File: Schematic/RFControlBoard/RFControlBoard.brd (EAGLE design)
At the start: 100 x 49 mm, 22 parts, among them IC1 LM320LZ-XX, U1 ATMEGA328P-PU

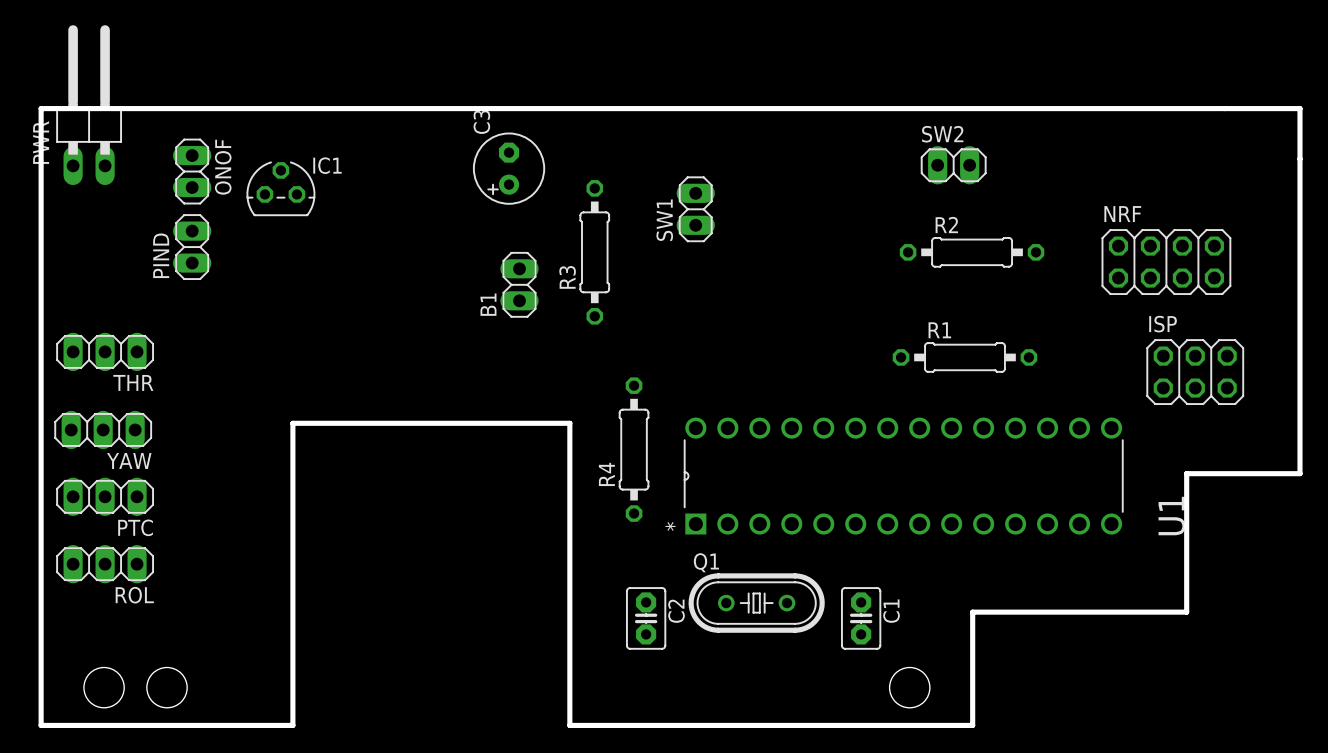
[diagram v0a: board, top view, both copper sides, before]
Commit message: Разведено для однослойной платы + пары проводков.
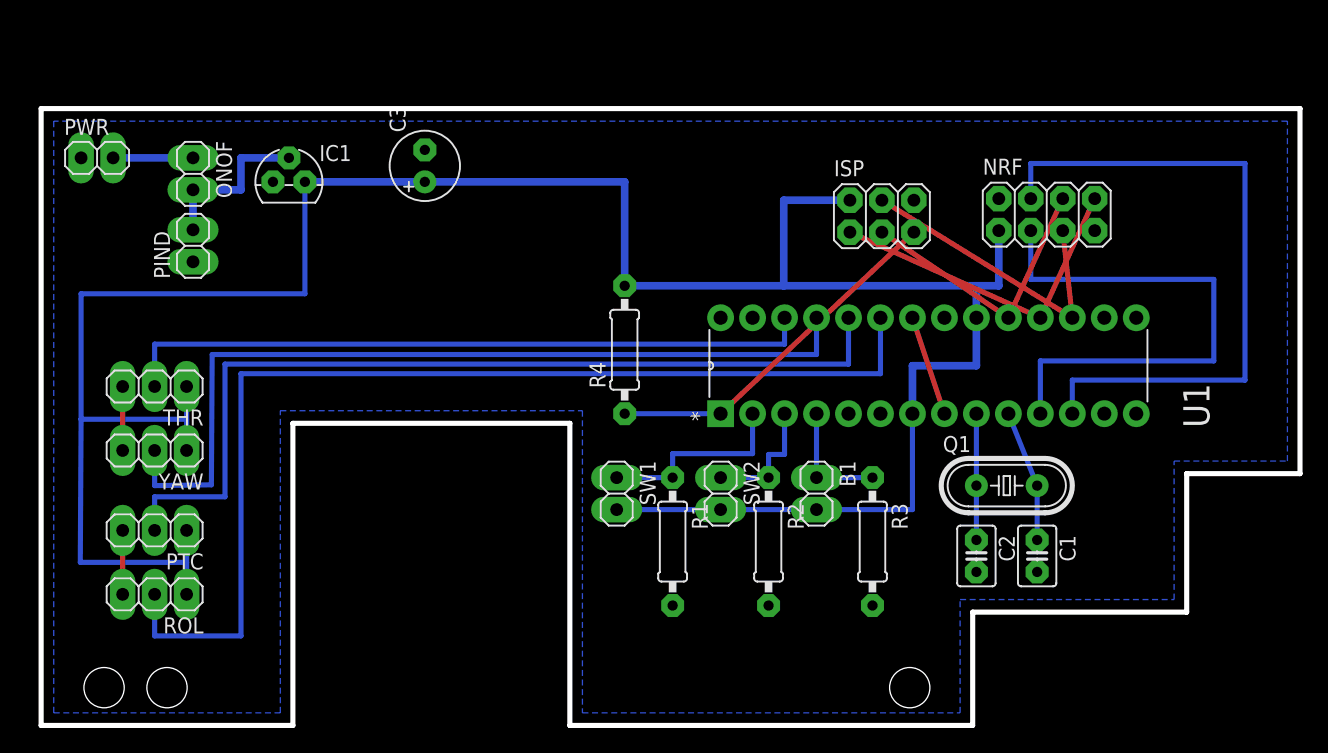
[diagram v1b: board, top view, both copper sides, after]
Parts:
- PWR: device pinhead:1X02/90 -> pinhead:1X02
- moved SW2 32.0 mm to (54.0, 18.4), turned to 270 degrees
- moved R3 31.9 mm to (66.0, 14.6), turned to 270 degrees
- moved B1 28.8 mm to (61.6, 18.4), turned to 270 degrees
- moved R2 28.1 mm to (57.8, 14.6), turned to 270 degrees
- moved ISP 27.8 mm to (66.8, 40.5)
- moved R1 27.4 mm to (50.2, 14.6), turned to 270 degrees
- moved C2 26.7 mm to (74.3, 13.5)
- moved SW1 23.4 mm to (45.7, 18.4), turned to 270 degrees
- moved Q1 21.9 mm to (76.7, 19.1)
- moved C1 14.8 mm to (79.1, 13.5)
- moved NRF 10.2 mm to (79.9, 40.6)
- moved U1 8.98 mm to (87.0, 32.4)
- moved R4 7.97 mm to (46.4, 29.8)
- moved C3 6.69 mm to (30.5, 44.5)
- moved THR 4.80 mm to (9.02, 26.9)
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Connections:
- net PTC: now also U1.24; no longer U1.26
- net ROL: now also U1.23; no longer U1.25
- net THR: now also U1.26; no longer U1.23
- net YAW: now also U1.25; no longer U1.24
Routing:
- net +3V3: track 0.00 -> 201.2 mm
- net ROL: track 0.00 -> 86.2 mm
- net PTC: track 0.00 -> 72.0 mm
- net YAW: track 0.00 -> 68.6 mm
- net THR: track 0.00 -> 55.5 mm
- net CE: track 0.00 -> 53.4 mm
- net CSN: track 0.00 -> 42.9 mm
- net RST: track 0.00 -> 28.7 mm
- net MISO: track 0.00 -> 27.0 mm
- net MOSI: track 0.00 -> 24.7 mm
- net SCK: track 0.00 -> 22.5 mm
- net GND: track 0.00 -> 18.2 mm
- net B1: track 0.00 -> 15.9 mm
- net N$3: track 0.00 -> 13.3 mm
- net N$7: track 0.00 -> 10.5 mm
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- added copper zone on layer 16, net GND
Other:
- outline, holes or cut-outs redrawn

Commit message: RC Control board (RCCB): 1) Schematic is updated for laser ironing PCB production :) 2) Initial version of RCCB firmware (3.3v 8Mhz). not tested.
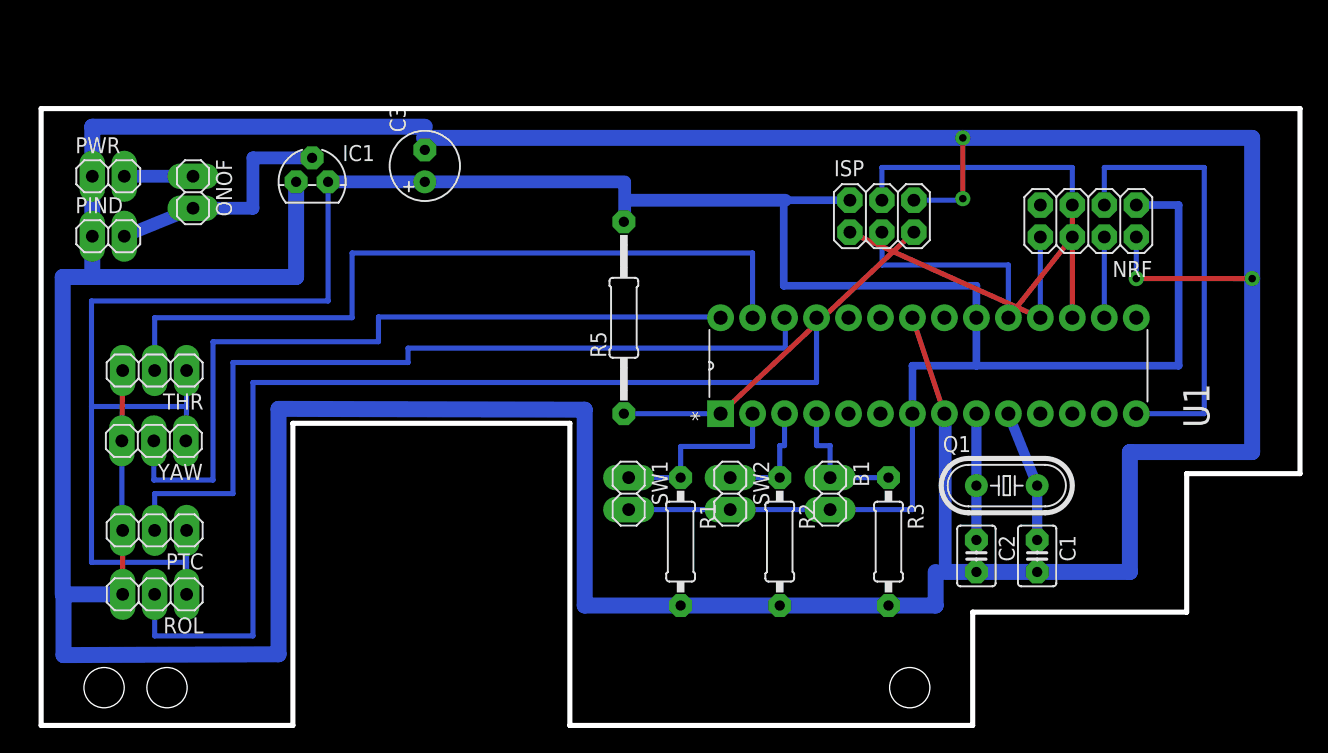
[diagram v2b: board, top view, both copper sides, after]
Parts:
- removed R4: 10K, rcl:0207/10
- added R5: 10K, rcl:0207/15
- moved PIND 6.77 mm to (5.33, 38.9), turned to 0 degrees
- moved NRF 3.34 mm to (83.2, 40.1), turned to 180 degrees
- moved IC1 1.84 mm to (21.5, 43.2)
- moved PWR 1.71 mm to (5.33, 43.6)
- moved ONOF 1.46 mm to (12.1, 42.4)
- moved THR 1.27 mm to (9.02, 28.2)
- moved R3 1.27 mm to (67.3, 14.6)
- moved B1 1.08 mm to (62.7, 18.4)
- moved SW1 0.95 mm to (46.7, 18.4)
- moved R2 0.89 mm to (58.7, 14.6)
- moved YAW 0.76 mm to (8.95, 22.6)
- moved SW2 0.76 mm to (54.7, 18.4)
- moved R1 0.63 mm to (50.8, 14.6)
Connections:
- removed net SCL: U1.28
- removed net SDA: U1.27
- net +3V3: now also R5.2; no longer R4.2
- net CE: now also U1.16; no longer U1.12
- net CSN: now also U1.14; no longer U1.11
- net PTC: now also U1.26; no longer U1.24
- net ROL: now also U1.25; no longer U1.23
- net RST: now also R5.1; no longer R4.1
- net THR: now also U1.27; no longer U1.26
- net YAW: now also U1.28; no longer U1.25
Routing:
- net GND: track 18.2 -> 395.1 mm, vias 0 -> 4
- net CE: track 53.4 -> 6.41 mm
- net +3V3: track 201.2 -> 219.3 mm
- net N$5: track 0.00 -> 12.9 mm
- net YAW: track 68.6 -> 61.2 mm
- net CSN: track 42.9 -> 35.9 mm
- net THR: track 55.5 -> 62.0 mm
- net N$3: track 13.3 -> 19.4 mm
- net ROL: track 86.2 -> 81.2 mm
- net PTC: track 72.0 -> 67.1 mm
- net MOSI: track 24.7 -> 29.7 mm
- net MISO: track 27.0 -> 23.0 mm
- net N$4: track 0.00 -> 3.05 mm
- net SCK: track 22.5 -> 25.0 mm
- net B3: track 9.53 -> 10.8 mm
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- removed copper zone on layer 16, net GND

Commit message: Temporary disable acc control.
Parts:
- C1, C2: value (none) -> 24pF
- C3: value (none) -> 100m
- Q1: value (none) -> 8MHz
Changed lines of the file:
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@@
 <attribute name="OC_FARNELL" value="1715487" x="94.615" y="64.135" size="1.778" layer="27" rot="R90" display="off"/>
 </element>
-<element name="Q1" library="crystal" package="HC49/S" value="" x="76.708" y="19.05">
+<element name="Q1" library="crystal" package="HC49/S" value="8MHz" x="76.708" y="19.05">
 <attribute name="OC_NEWARK" value="unknown" x="104.648" y="-30.48" size="1.778" layer="27" display="off"/>
 <attribute name="MPN" value="" x="104.648" y="-30.48" size="1.778" layer="27" display="off"/>
@@
 <attribute name="OC_FARNELL" value="1667008" x="104.648" y="-30.48" size="1.778" layer="27" display="off"/>
 </element>
-<element name="C1" library="capacitor-wima" package="C2.5-3" value="" x="79.121" y="13.462" rot="R270"/>
-<element name="C2" library="capacitor-wima" package="C2.5-3" value="" x="74.295" y="13.462" rot="R270"/>
+<element name="C1" library="capacitor-wima" package="C2.5-3" value="24pF" x="79.121" y="13.462" rot="R270"/>
+<element name="C2" library="capacitor-wima" package="C2.5-3" value="24pF" x="74.295" y="13.462" rot="R270"/>
 <element name="THR" library="pinhead" package="1X03" value="" x="9.017" y="28.194" rot="R180"/>
 <element name="YAW" library="pinhead" package="1X03" value="" x="8.9535" y="22.606" rot="R180"/>
@@
 <element name="PIND" library="pinhead" package="1X02" value="" x="5.334" y="38.862"/>
 <element name="IC1" library="linear" package="TO92" value="LM320LZ-XX" x="21.5265" y="43.18"/>
-<element name="C3" library="rcl" package="E2,5-6" value="" x="30.48" y="44.45" rot="R90"/>
+<element name="C3" library="rcl" package="E2,5-6" value="100m" x="30.48" y="44.45" rot="R90"/>
 <element name="ISP" library="pinhead" package="2X03" value="" x="66.788" y="40.4525"/>
 <element name="R1" library="rcl" package="0207/10" value="10K" x="50.8" y="14.605" rot="R270"/>
